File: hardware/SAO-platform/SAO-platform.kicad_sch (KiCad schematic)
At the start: 28 parts, among them U1 WCH CH32V003F4U6

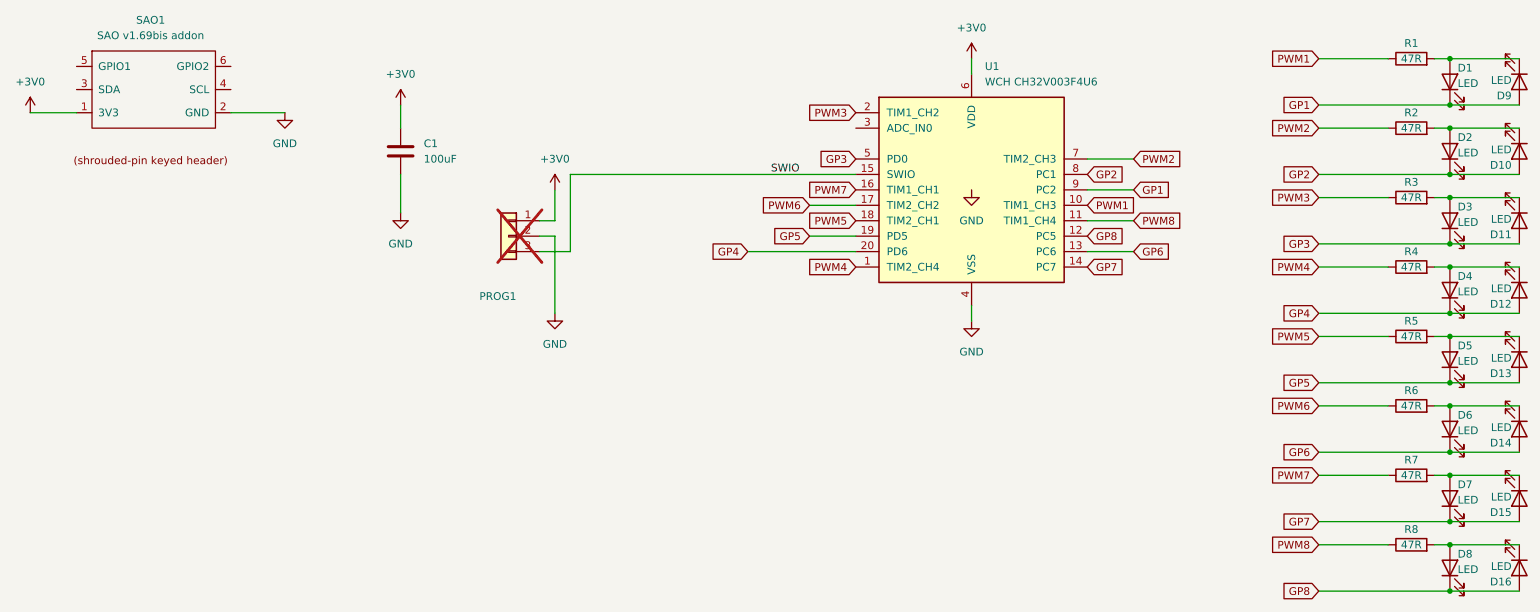
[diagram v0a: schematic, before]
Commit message: layout complete, passes DRC
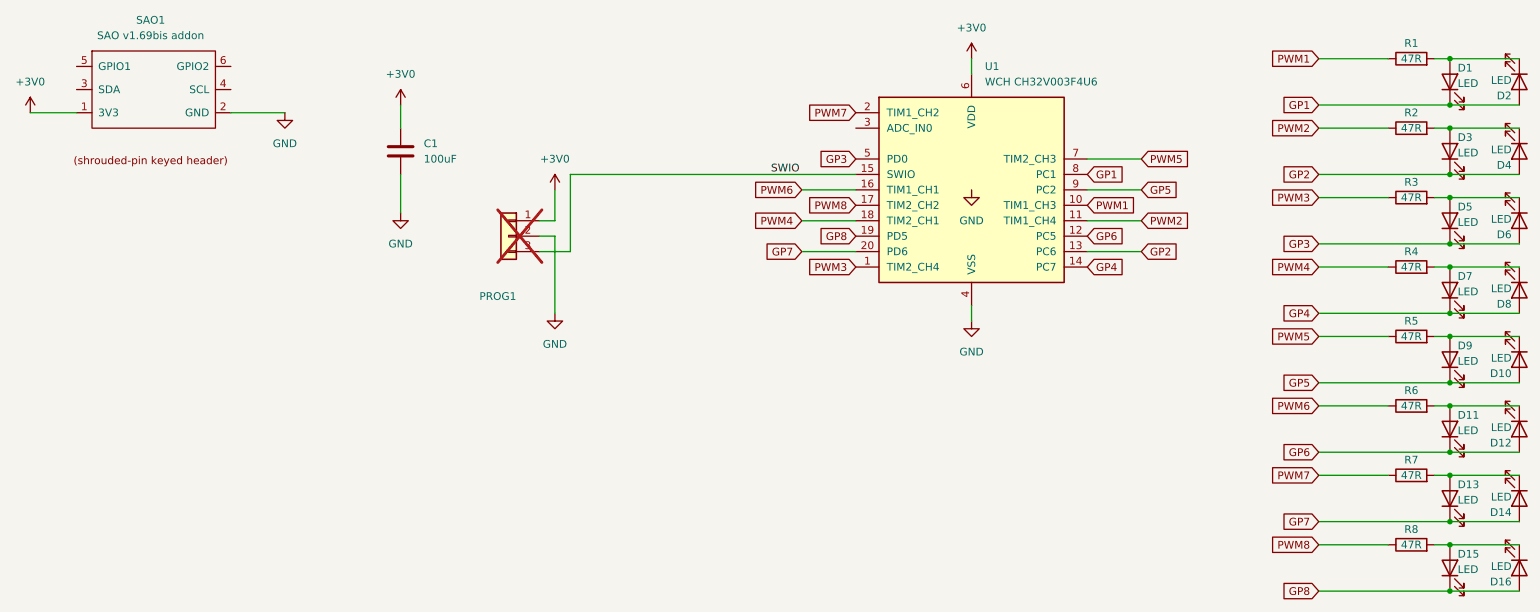
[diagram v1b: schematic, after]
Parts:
- renumbered D13 to D10, D6 to D11, D14 to D12, D7 to D13, D15 to D14, D8 to D15, D9 to D2, D2 to D3, D10 to D4, D3 to D5, D11 to D6, D4 to D7, D12 to D8, D5 to D9
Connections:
- net GP1: now also U1.8 (PC1); no longer U1.9 (PC2)
- net GP2: now also U1.13 (PC6); no longer U1.8 (PC1)
- net GP4: now also U1.14 (PC7); no longer U1.20 (PD6)
- net GP5: now also U1.9 (PC2); no longer U1.19 (PD5)
- net GP6: now also U1.12 (PC5); no longer U1.13 (PC6)
- net GP7: now also U1.20 (PD6); no longer U1.14 (PC7)
- net GP8: now also U1.19 (PD5); no longer U1.12 (PC5)
- net PWM2: now also U1.11 (PC4); no longer U1.7 (PC0)
- net PWM3: now also U1.1 (PD7); no longer U1.2 (PA1)
- net PWM4: now also U1.18 (PD4); no longer U1.1 (PD7)
- net PWM5: now also U1.7 (PC0); no longer U1.18 (PD4)
- net PWM6: now also U1.16 (PD2); no longer U1.17 (PD3)
- net PWM7: now also U1.2 (PA1); no longer U1.16 (PD2)
- net PWM8: now also U1.17 (PD3); no longer U1.11 (PC4)

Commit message: shrunk to 8mm grid for LED centres
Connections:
- net PWM3: now also U1.7 (PC0); no longer U1.1 (PD7)
- net PWM4: now also U1.17 (PD3); no longer U1.18 (PD4)
- net PWM5: now also U1.2 (PA1); no longer U1.7 (PC0)
- net PWM7: now also U1.1 (PD7); no longer U1.2 (PA1)
- net PWM8: now also U1.18 (PD4); no longer U1.17 (PD3)
